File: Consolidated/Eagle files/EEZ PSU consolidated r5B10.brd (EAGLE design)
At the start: 309 x 150 mm, 554 parts, among them IC1 LTC3864EMSE#PBF, IC10 REF5025AIDG4, IC11 DAC8552IDGKTG4, IC12 ADG465SOT-23, IC13 TS5A9411DCKT, IC14 ADS1120IPWR, IC15 LP339D, IC16 LM25575MH/NOPB, IC17 TPD4E002DRLR, IC18 TPD2E001DZDR, IC19 ADUM3160BRWZ, IC2 MC79L05, IC20 TLC5925IDBQR, IC21 Si8641EC-B-IS1, IC22 SI8651EC-B-IS1, IC23 SI8651EC-B-IS1, IC24 LD1117ADT33TR, IC25 Si8641EC-B-IS1, IC26 PCA21125T/Q900/1,1, IC27 AT25256B-SSHL-B, IC28 W5500, IC29 BC857BS, IC3 MC78L05, IC30 TLC555, IC31 SN74LVC2G08DCTR, IC32 TPS3705-33D, IC33 SN74LV1T34DBVR, IC34 SN74LVC2G02DCTR, IC4 LM5574MTX/NOPB, IC5 LP2951SO8, IC6 TL072D, IC7 TL072D, IC8 OP27GSZ, IC9 MCP23S08-E/SO, J1 BS-244DSM-R, J2 BS-244DSM-G, J3 BS-244DSM-B, J4 BS-244DSM-R, J5 BS-244DSM-B, Q1 IRFR5305, Q10 MMBT5401, Q11 MMBT5401, Q12 MMBT5551, Q13 MMBT5551, Q14 BSS84P, Q15 2N7002, Q16 MMBT5551, Q17 MMBT5401, Q18 MMBT5551, Q19 MMBT5551, Q2 MMBT5401, Q20 BTA26-600, Q21 BTA26-600, Q22 IRLL014N, Q23 IRLML2246TRPBF, Q24 IRLML2246TRPBF, Q25 IRLML2246TRPBF, Q26 IRLML2246TRPBF, Q27 2N7002, Q28 IRLML2246TRPBF, Q29 2N7002, Q3 2N7002, Q30 2N7002, Q4 IRFP250N, Q5 BC857C, Q6 BC846C, Q7 BCP56-16.115, Q8 IRFR5410, Q9 BCP56-16.115, SW1 A101SYCQ04, SW2 1301.9316, X1 39303035, X10 826629-5, X11 2411-01, X12 MC000006, X13 TSW-113-07-F-D, X14 MC000005, X15 TSW-113-07-F-D, X16 09185067324, X17 22-23-2021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

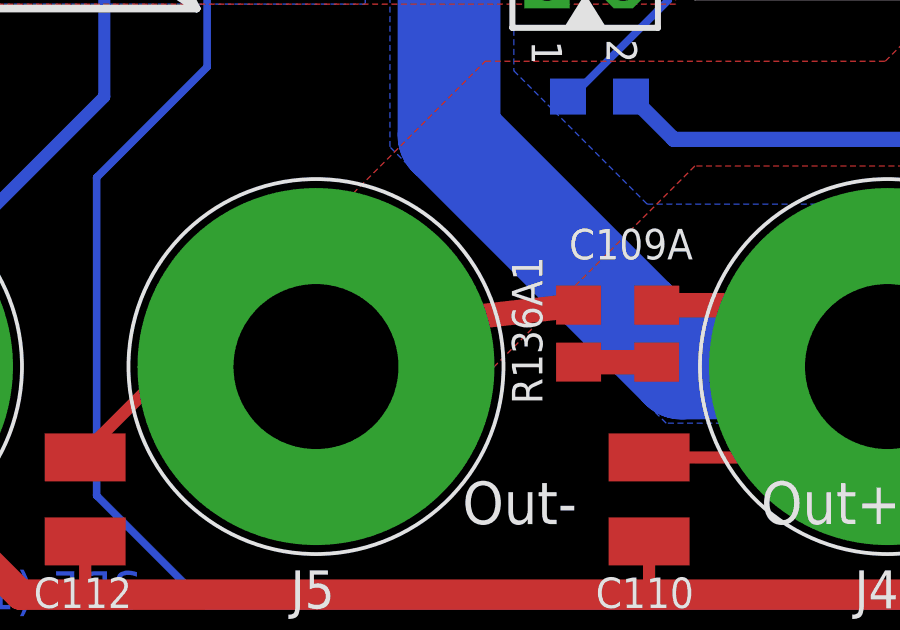
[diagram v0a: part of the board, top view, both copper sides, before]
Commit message: r5B10 BOM, top silkscreen minor correction
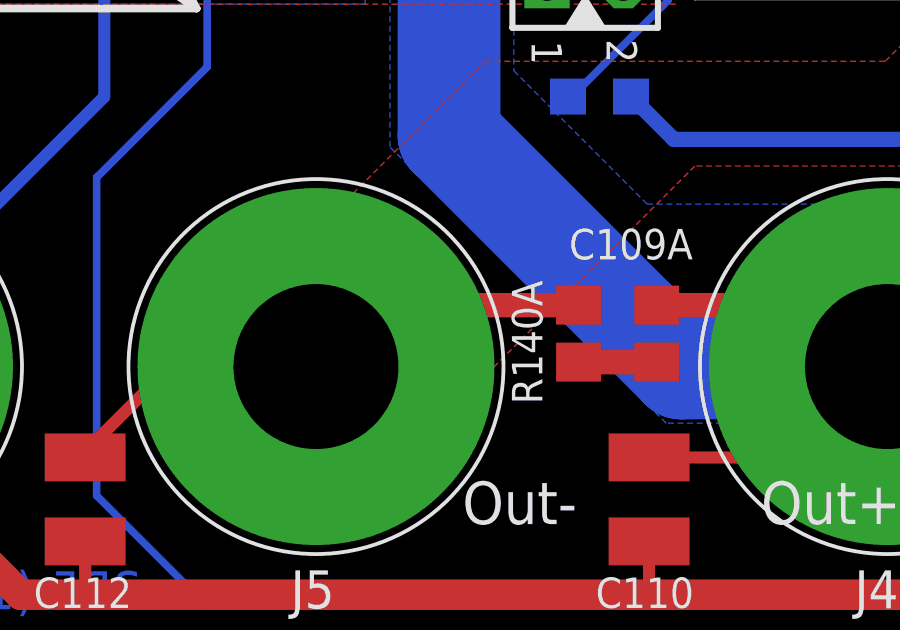
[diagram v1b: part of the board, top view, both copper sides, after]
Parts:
- renumbered R136A1 to R140A
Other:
- board text added: "R140A"
- board text removed: "R136A1"
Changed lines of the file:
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@@
 <layer number="23" name="tOrigins" color="15" fill="1" visible="yes" active="yes"/>
 <layer number="24" name="bOrigins" color="15" fill="1" visible="no" active="yes"/>
-<layer number="25" name="tNames" color="7" fill="1" visible="no" active="yes"/>
+<layer number="25" name="tNames" color="7" fill="1" visible="yes" active="yes"/>
 <layer number="26" name="bNames" color="13" fill="1" visible="no" active="yes"/>
 <layer number="27" name="tValues" color="10" fill="1" visible="no" active="yes"/>
@@
 <text x="183.7055" y="28.1305" size="1.016" layer="125" ratio="10">R136</text>
 <text x="179.959" y="7.62" size="1.016" layer="125" ratio="10" rot="R90">R136A</text>
-<text x="141.097" y="7.747" size="1.016" layer="125" ratio="10" rot="R90">R136A1</text>
+<text x="141.097" y="7.747" size="1.016" layer="125" ratio="10" rot="R90">R140A</text>
 <text x="158.26389375" y="52.269390625" size="0.9906" layer="125" ratio="10">R137</text>
 <text x="163.5394" y="67.20489375" size="0.9906" layer="125" ratio="10">R138</text>
@@
 <attribute name="VALUE" x="144.2085" y="11.3665" size="1.27" layer="27" rot="R270"/>
 </element>
-<element name="R136A1" library="rcl" package="R0805" value="1R" x="142.3035" y="10.0965" smashed="yes" rot="R270">
+<element name="R140A" library="rcl" package="R0805" value="1R" x="142.3035" y="10.0965" smashed="yes" rot="R270">
 <attribute name="NAME" x="141.097" y="7.747" size="1.016" layer="25" ratio="10" rot="R90"/>
 <attribute name="VALUE" x="141.732" y="11.43" size="1.27" layer="27" rot="R270"/>
@@
 <contactref element="C112" pad="2"/>
 <wire x1="125.857" y1="5.972" x2="125.4125" y2="5.718" width="0.4064" layer="1"/>
-<contactref element="R136A1" pad="1"/>
-<wire x1="142.3035" y1="11.0465" x2="134.4905" y2="10.1575" width="0.8128" layer="1"/>
-<wire x1="134.4905" y1="10.1575" x2="133.731" y2="9.398" width="0.8128" layer="1"/>
+<contactref element="R140A" pad="1"/>
+<wire x1="142.3035" y1="11.0465" x2="135.3795" y2="11.0465" width="0.8128" layer="1"/>
+<wire x1="135.3795" y1="11.0465" x2="133.731" y2="9.398" width="0.8128" layer="1"/>
 </signal>
 <signal name="N$306">
@@
 <signal name="N$178">
 <contactref element="C109A" pad="2"/>
-<contactref element="R136A1" pad="2"/>
+<contactref element="R140A" pad="2"/>
 <wire x1="142.3035" y1="9.1465" x2="144.907" y2="9.1465" width="0.8128" layer="1"/>
 </signal>
@@
 </signal>
 </signals>
-<errors>
-</errors>
 </board>
 </drawing>
